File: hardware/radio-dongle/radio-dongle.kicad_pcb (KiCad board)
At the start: 4 copper layers, 82.4 x 52.1 mm, 34 parts, among them J2 Conn_01x15, J3 AVR-JTAG-10, SW1 SW_Push, U1 SN65HVD230, U2 STM32F103C8T6, Y1 12mhz

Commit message: i can't believe what they did to my boy
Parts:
- removed C1, C10, C3, C4, C5, C6, C7: 100nf, Capacitor_SMD:C_0402_1005Metric
- removed C2: 4.7nf, Capacitor_SMD:C_0805_2012Metric
- removed C8, C9: C_Small, Capacitor_SMD:C_0402_1005Metric
- removed D1: GRN, LED_SMD:LED_0603_1608Metric
- removed D2: RED, LED_SMD:LED_0603_1608Metric
- removed J3: AVR-JTAG-10, Connector_PinHeader_1.27mm:PinHeader_2x06_P1.27mm_Vertical_SMD
- removed JP1, JP2: Jumper_3_Open, Jumper:SolderJumper-3_P1.3mm_Open_Pad1.0x1.5mm_NumberLabels
- removed R1: 120,DNP, Resistor_SMD:R_0805_2012Metric
- removed R2, R4: 240R, Resistor_SMD:R_0603_1608Metric
- removed R3: 10k, Resistor_SMD:R_0402_1005Metric
- removed R5, R6: 100k, Resistor_SMD:R_0402_1005Metric
- removed the REF** at (137.4, 74.2)
- removed the REF** at (72.1, 108.7)
- removed the REF** at (137.4, 73.9)
- removed the REF** at (159.3, 103.1)
- removed the REF** at (100.8, 108.7)
- removed SW1: SW_Push, ConeCodes:SW_RS-032G05A3-SMRT
- removed U1: SN65HVD230, Package_SO:SOIC-8_3.9x4.9mm_P1.27mm
- removed U2: STM32F103C8T6, Package_QFP:LQFP-48_7x7mm_P0.5mm
- removed Y1: 12mhz, Crystal:Crystal_SMD_3225-4Pin_3.2x2.5mm
- added REF**: BBQ10KBD, ConeCodes:BBQ10KBD, B.Cu at (83.8, 120.3)
- J2: moved to B.Cu
- moved AE2 83.9 mm to (74.5, 51.4), turned to 180 degrees
- moved AE1 66.4 mm to (89.5, 51.4), turned to 180 degrees
- moved REF** 59.8 mm to (106.5, 53.9), turned to 180 degrees
- moved J2 10.5 mm to (82.5, 81.5)
- renumbered AE2 to AE1
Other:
- board size 82.4 x 52.1 mm -> 67 x 91.5 mm

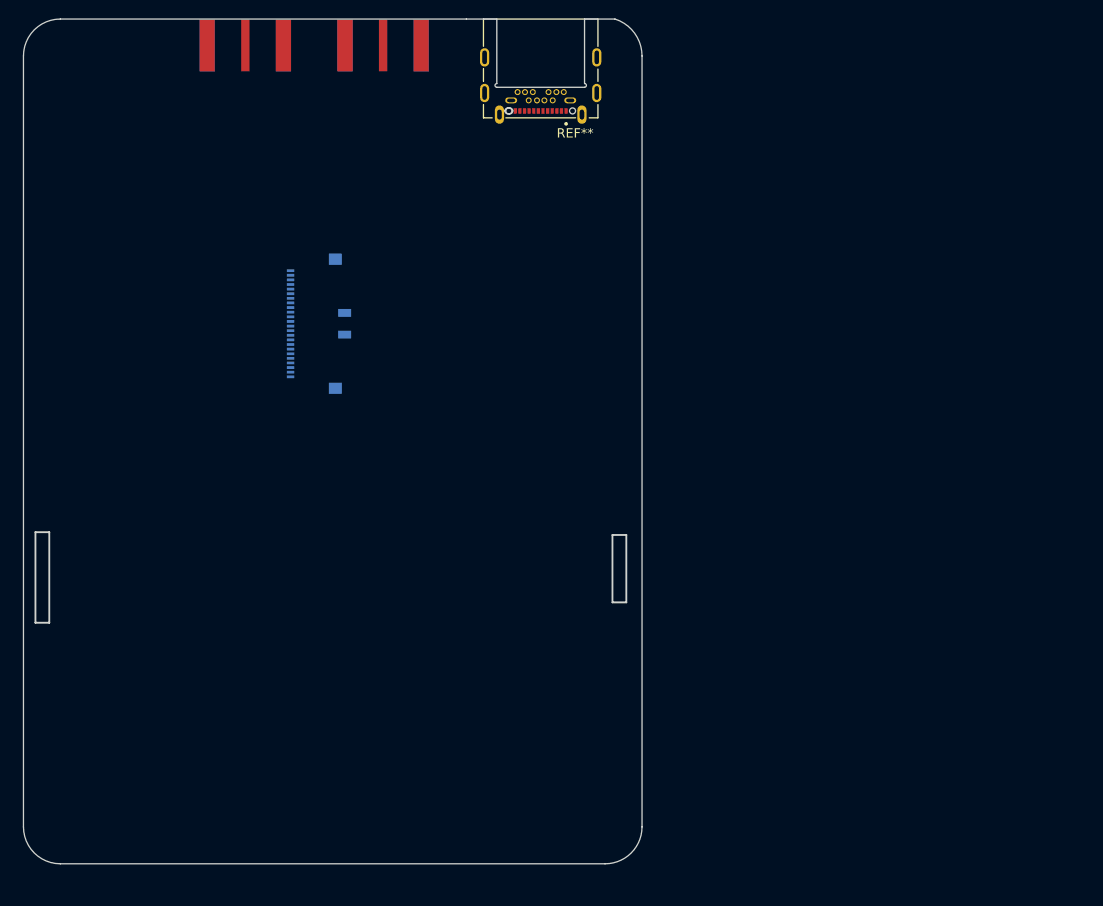
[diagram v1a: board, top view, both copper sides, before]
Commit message: Hardware updates
* fix messed up +12v pin
* add a ground output for neopixels on both channels
* add a i2c microphone
* clean up schematic
* calculate component values for the LED drivers
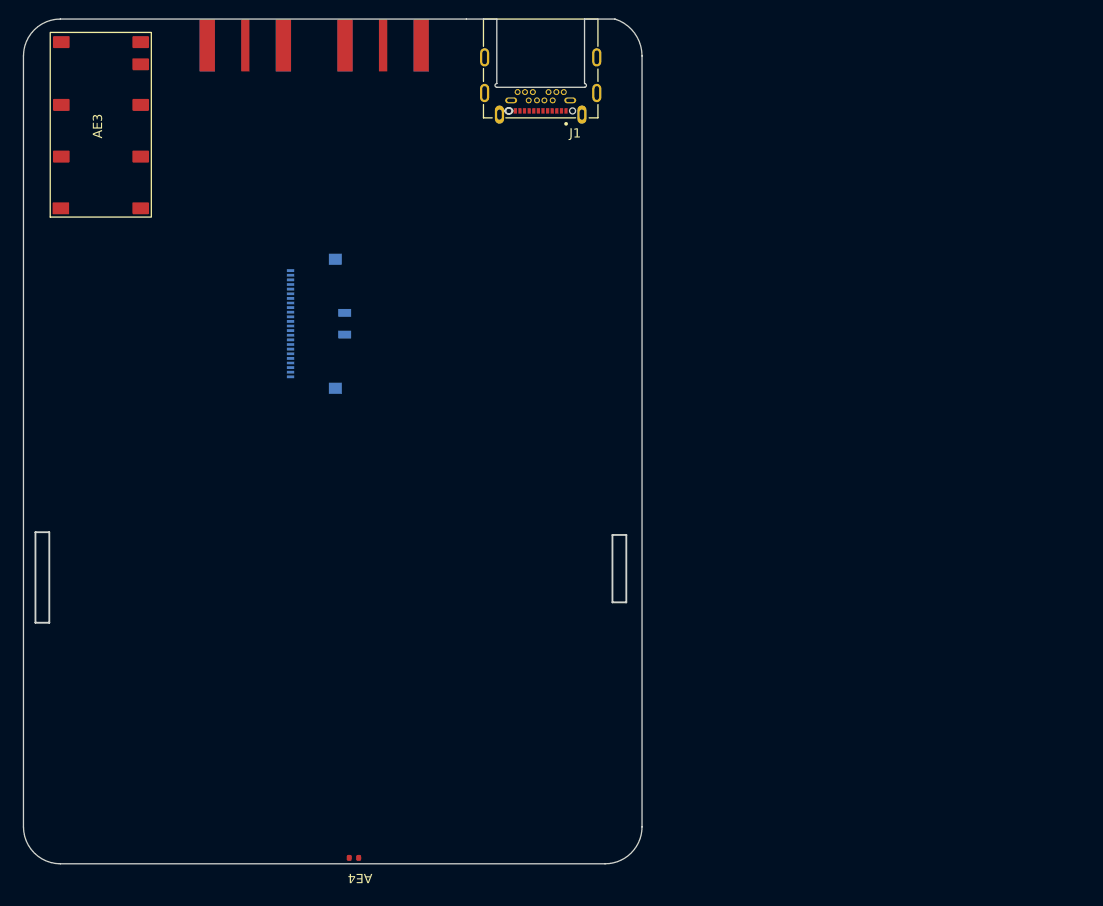
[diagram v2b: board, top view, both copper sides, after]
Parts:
- added AE3: Antenna_Chip_MP, ConeCodes:SR4C033-L, F.Cu at (58.0, 60.4)
- added AE4: Antenna_Chip, ConeCodes:SRCW004, F.Cu at (86.8, 139.1)
- renumbered REF** to J1
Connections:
- AE1 pad 1: unconnected-(AE2-Pad1) -> unconnected-(AE1-Pad1)
- AE1 pad 2: unconnected-(AE2-Pad2) -> unconnected-(AE1-Pad2)
